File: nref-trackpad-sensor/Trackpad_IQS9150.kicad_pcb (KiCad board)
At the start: 2 copper layers, 89 x 52.8 mm, 49 parts, among them CN1 FPC_6PIN, IC1 IQS9150-000QFR

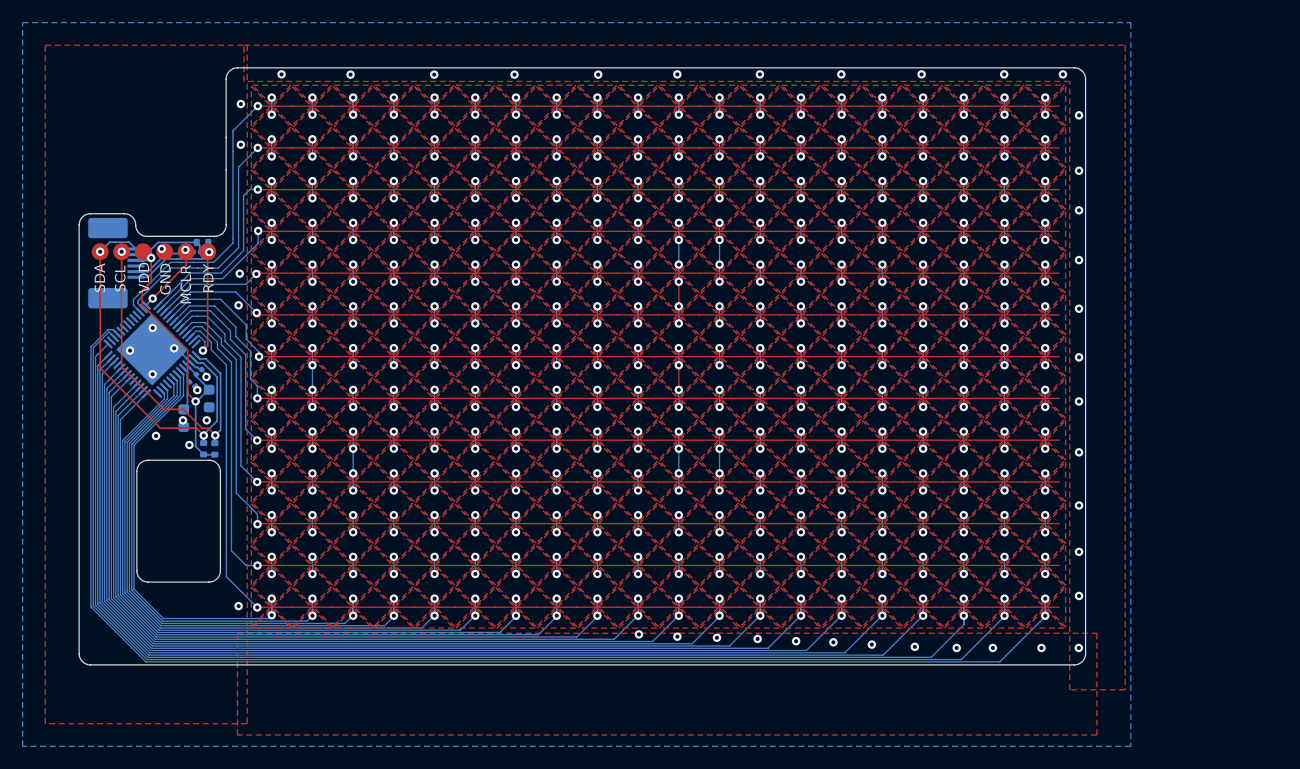
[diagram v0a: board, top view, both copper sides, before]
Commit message: trackpad sensor: redesign pcb shape for production
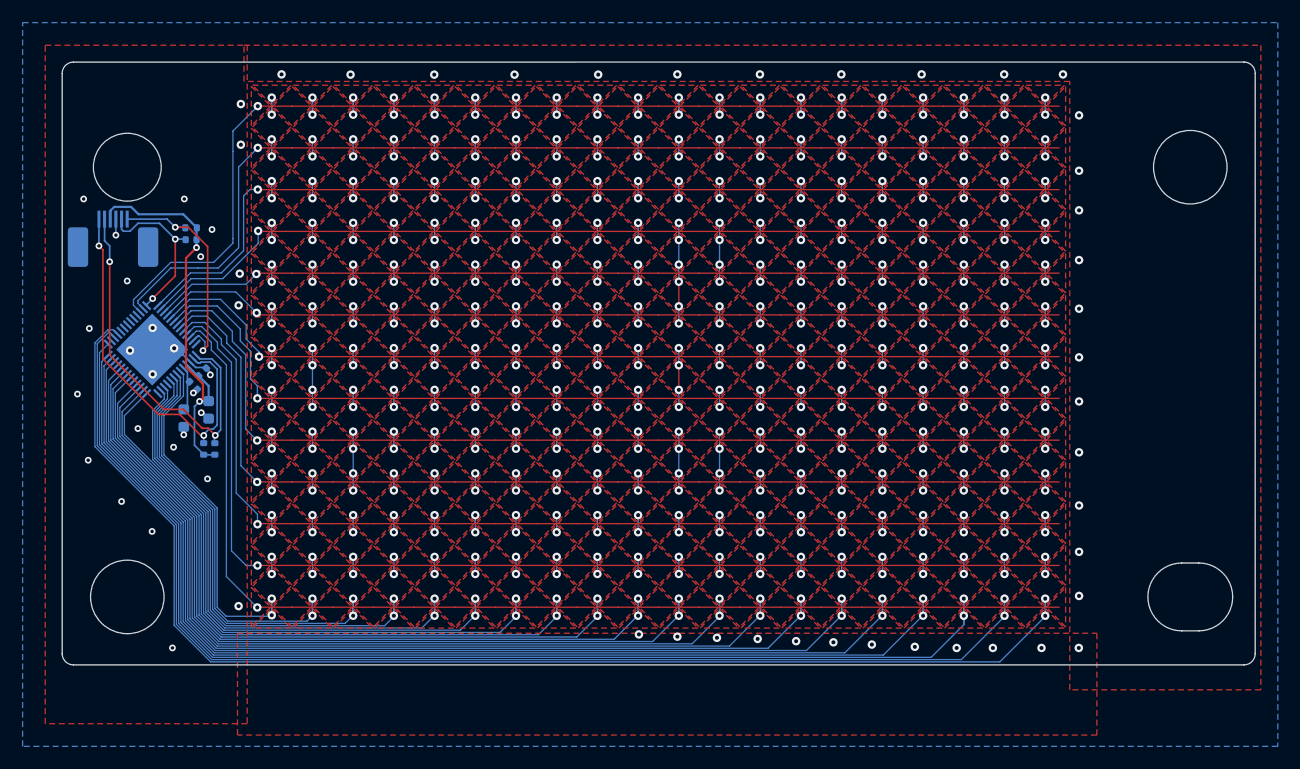
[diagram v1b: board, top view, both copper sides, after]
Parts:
- removed TP1, TP2, TP3, TP4, TP5, TP6: TESTPOINTROUND1.5MMNO, Trackpad_IQS9150:TESTPOINT_ROUND_1.5MM_NO
- added H1: BADGE, footprints:nref-tpsensor-badge, B.Cu at (202.0, 106.5)
- C2, C4, C5: footprint Capacitor_SMD:C_0201_0603Metric -> Capacitor_SMD:C_0402_1005Metric
- moved CN1 3.04 mm to (107.0, 93.0), turned to 180 degrees
- moved R1 1.64 mm to (113.9, 92.8), turned to 0 degrees
- moved C5 1.21 mm to (113.9, 93.8)
- moved C1 1.01 mm to (115.5, 108.8)
- moved C2 0.30 mm to (114.9, 105.5)
- moved C4 0.14 mm to (114.1, 106.7)
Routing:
- net /Trackpad_IQS9150_1/COL1: track 54.3 -> 48.5 mm
- net /Trackpad_IQS9150_1/COL3: track 65.3 -> 59.8 mm
- net /Trackpad_IQS9150_1/COL2: track 60.4 -> 54.8 mm
- net /Trackpad_IQS9150_1/COL6: track 72.4 -> 66.8 mm
- net /Trackpad_IQS9150_1/COL5: track 68.7 -> 63.1 mm
- net /Trackpad_IQS9150_1/COL4: track 65.4 -> 59.8 mm
- net /Trackpad_IQS9150_1/COL19: track 129.4 -> 125.8 mm
- net /Trackpad_IQS9150_1/COL20: track 134.0 -> 130.4 mm
- net /Trackpad_IQS9150_1/COL18: track 124.8 -> 121.1 mm
- net /Trackpad_IQS9150_1/COL17: track 118.4 -> 114.7 mm
- net /Trackpad_IQS9150_1/COL16: track 114.1 -> 110.5 mm
- net /Trackpad_IQS9150_1/COL15: track 109.9 -> 106.3 mm
- net /Trackpad_IQS9150_1/COL14: track 105.4 -> 101.8 mm
- net /Trackpad_IQS9150_1/COL13: track 101.1 -> 97.5 mm
- net /Trackpad_IQS9150_1/COL12: track 101.3 -> 97.7 mm
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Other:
- board size 89 x 52.8 mm -> 105.5 x 53.3 mm
- board text removed: "GND"
- board text removed: "MCLR"
- board text removed: "RDY"
- board text removed: "SCL"
- board text removed: "SDA"
- board text removed: "VDD"
